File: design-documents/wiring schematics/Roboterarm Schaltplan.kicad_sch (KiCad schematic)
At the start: 5 parts

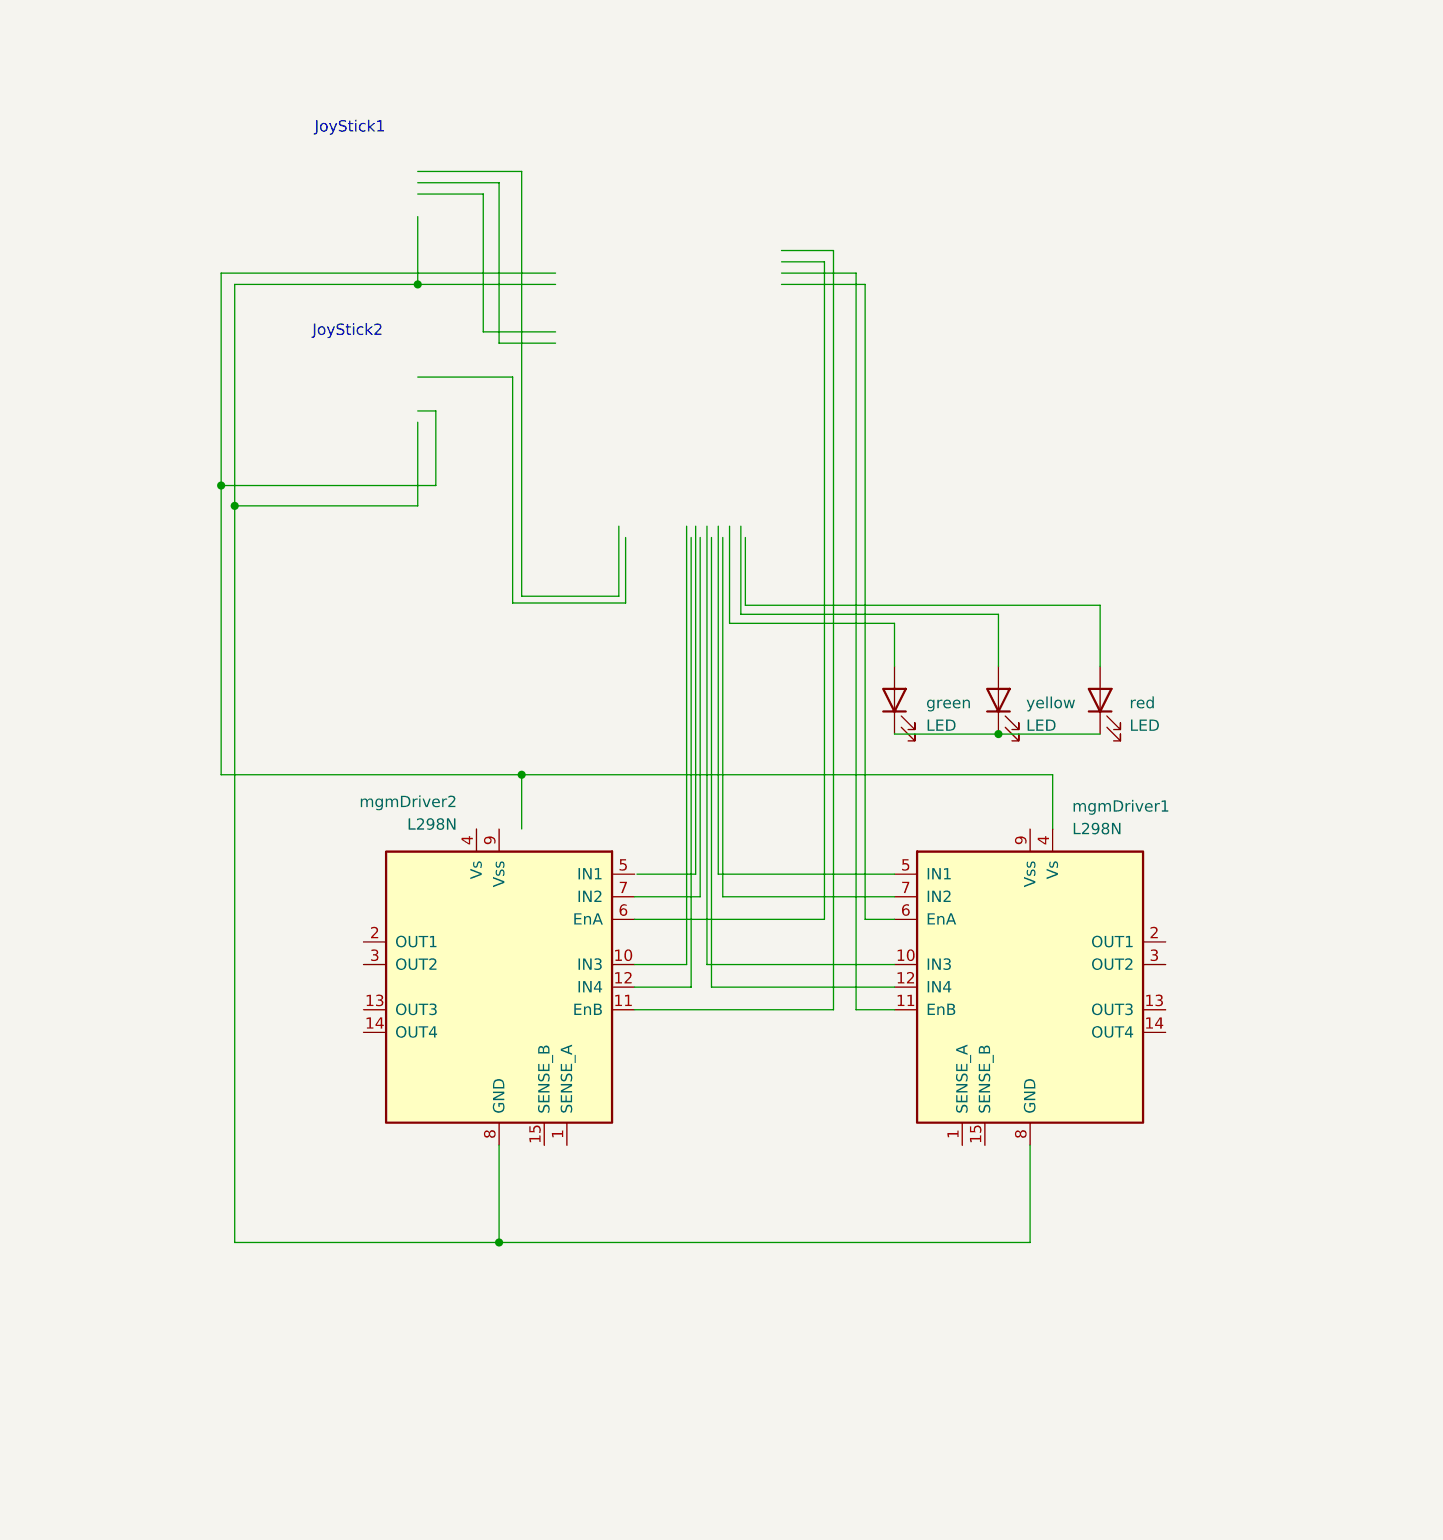
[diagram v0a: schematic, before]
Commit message: Schaltplan fertiggestellt.
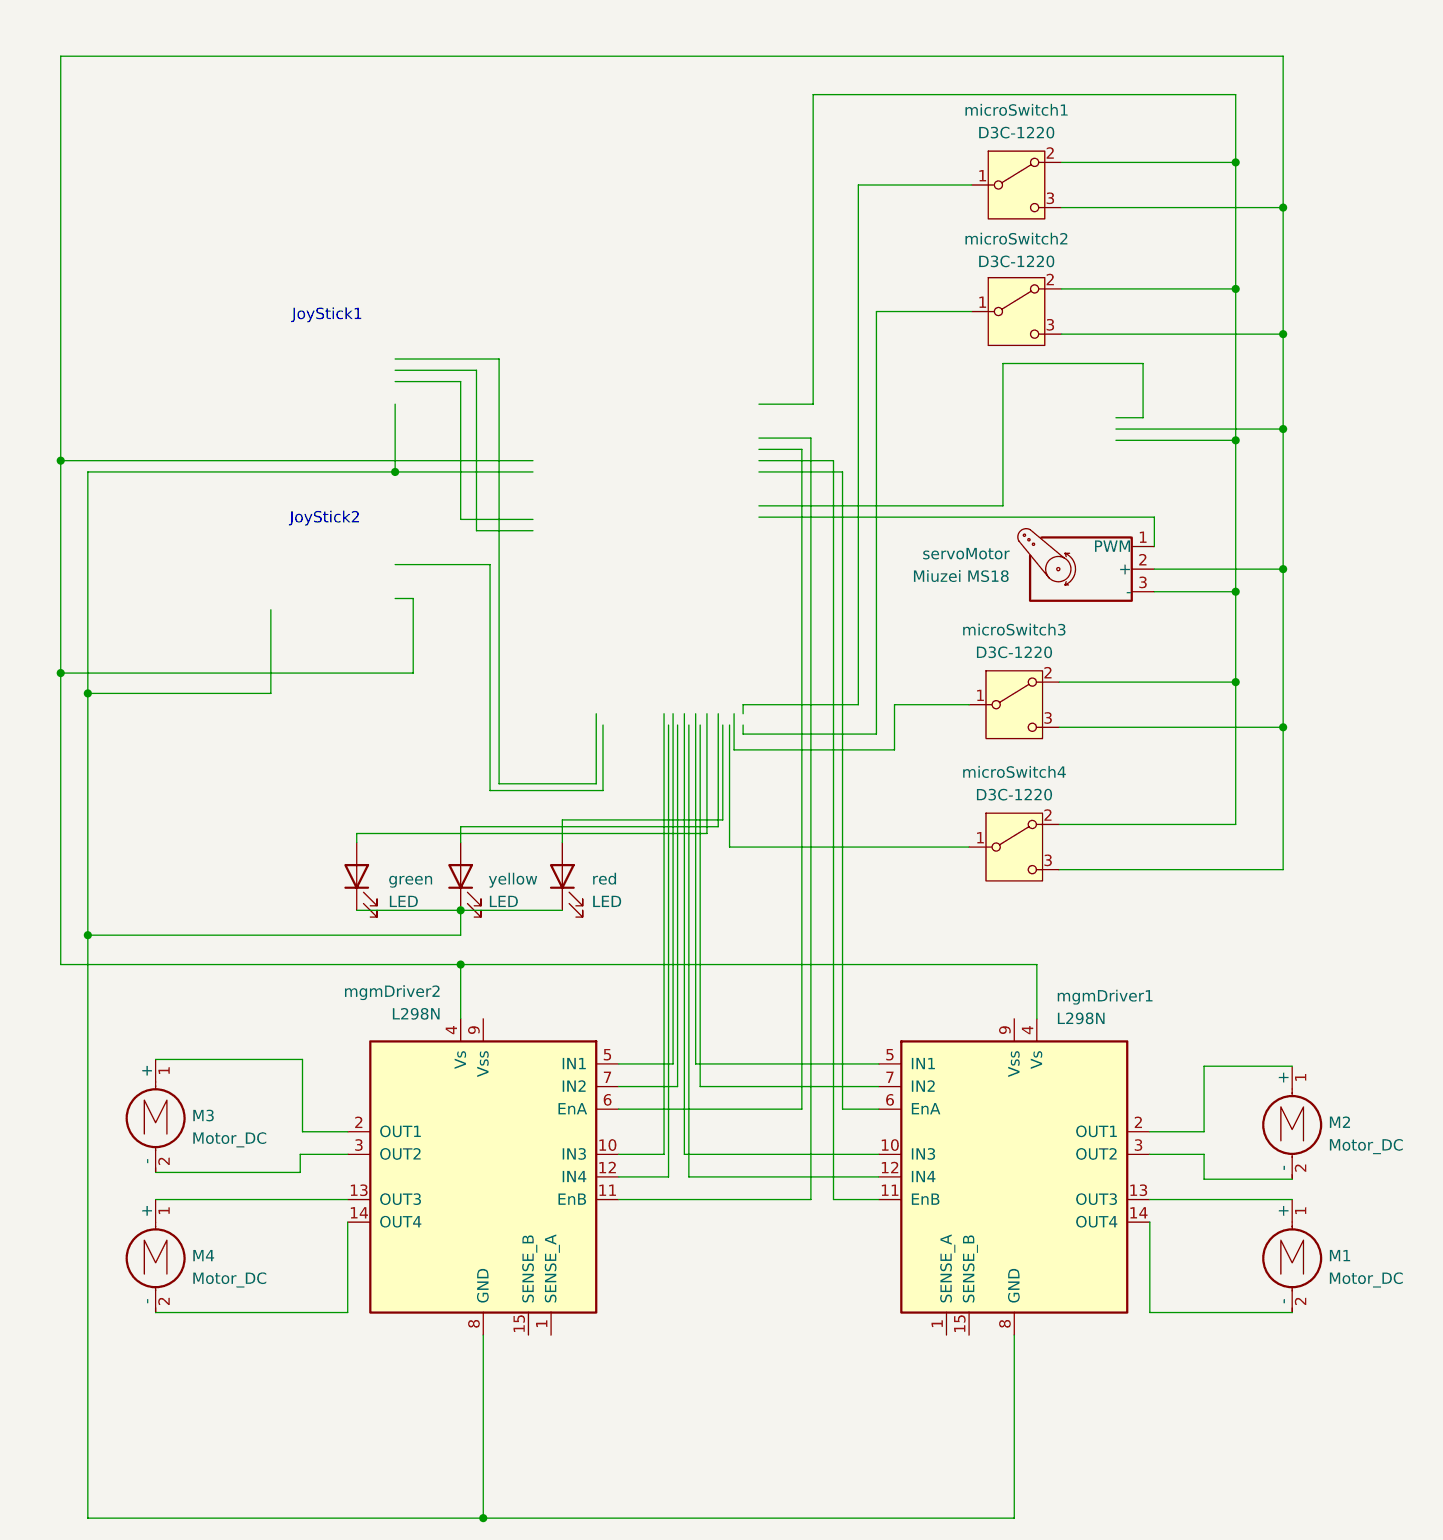
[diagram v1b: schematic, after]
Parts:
- added M1, M2, M3, M4: Motor_DC, symbol Motor:Motor_DC
- added microSwitch1, microSwitch2, microSwitch3, microSwitch4: D3C-1220, Button_Switch_THT:SW_Slide-03_Wuerth-WS-SLTV_10x2.5x6.4_P2.54mm, symbol Switch:SW_Wuerth_450301014042
- added servoMotor: Miuzei MS18, symbol Motor:Motor_Servo
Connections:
- net at mgmDriver1.13 (OUT3): now also M1.1 (+)
- net at mgmDriver1.14 (OUT4): now also M1.2 (-)
- net at mgmDriver1.2 (OUT1): now also M2.1 (+)
- net at mgmDriver1.3 (OUT2): now also M2.2 (-)
- net at mgmDriver1.4 (Vs): now also mgmDriver2.4 (Vs), microSwitch1.3 (C), microSwitch2.3 (C), microSwitch3.3 (C), microSwitch4.3 (C), servoMotor.2 (+)
- net at mgmDriver1.8 (GND), mgmDriver2.8 (GND): now also green.1 (K), red.1 (K), yellow.1 (K)
- net at mgmDriver2.13 (OUT3): now also M4.1 (+)
- net at mgmDriver2.14 (OUT4): now also M4.2 (-)
- net at mgmDriver2.2 (OUT1): now also M3.1 (+)
- net at mgmDriver2.3 (OUT2): now also M3.2 (-)
- new net: microSwitch1.2 (A), microSwitch2.2 (A), microSwitch3.2 (A), microSwitch4.2 (A), servoMotor.3 (-)
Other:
- moved on the sheet: green, mgmDriver1, mgmDriver2, red, yellow

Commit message: Debugging.
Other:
- note added: "1...9"
- note added: "PS2_Controller_Port"
- note removed: "JoyStick1"
- note removed: "JoyStick2"
- moved on the sheet: green, red, yellow
